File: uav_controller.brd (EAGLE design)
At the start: 100 x 80 mm, 26 parts, among them IC1 PIC16F877SO, U1 L298, U2 L298, U3 LCD-16X28X2

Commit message: Renamed some components
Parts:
- removed R2, R3, R4, R5, R6, R7, R8: (no value), SparkFun-Resistors:AXIAL-0.3EZ
- OSC: value (none) -> 8Mhz
- renumbered R9 to BKLT, U1 to HBRIDGE-FRONT, U2 to HBRIDGE-REAR, Y1 to OSC
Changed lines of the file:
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@@
 <element name="PWRIN" library="SparkFun-Passives" package="1X02" value="" x="67.31" y="67.31" rot="R270"/>
 <element name="R1" library="SparkFun-Resistors" package="AXIAL-0.3EZ" value="" x="33.02" y="49.53" rot="R90"/>
-<element name="R2" library="SparkFun-Resistors" package="AXIAL-0.3EZ" value="" x="-27.94" y="57.15"/>
-<element name="R3" library="SparkFun-Resistors" package="AXIAL-0.3EZ" value="" x="-38.1" y="57.15"/>
-<element name="R4" library="SparkFun-Resistors" package="AXIAL-0.3EZ" value="" x="-48.26" y="57.15"/>
-<element name="R5" library="SparkFun-Resistors" package="AXIAL-0.3EZ" value="" x="-17.78" y="60.96"/>
-<element name="R6" library="SparkFun-Resistors" package="AXIAL-0.3EZ" value="" x="-27.94" y="60.96"/>
-<element name="R7" library="SparkFun-Resistors" package="AXIAL-0.3EZ" value="" x="-38.1" y="60.96"/>
-<element name="R8" library="SparkFun-Resistors" package="AXIAL-0.3EZ" value="" x="-48.26" y="60.96"/>
-<element name="U1" library="SparkFun-PowerIC" package="MULTIWATT15" value="L298" x="58.42" y="30.48" rot="R270"/>
-<element name="U2" library="SparkFun-PowerIC" package="MULTIWATT15" value="L298" x="50.8" y="52.07" rot="R270"/>
+<element name="HBRIDGE-FRONT" library="SparkFun-PowerIC" package="MULTIWATT15" value="L298" x="58.42" y="30.48" rot="R270"/>
+<element name="HBRIDGE-REAR" library="SparkFun-PowerIC" package="MULTIWATT15" value="L298" x="50.8" y="52.07" rot="R270"/>
 <element name="U3" library="SparkFun-Displays" package="LCD-8X2" value="LCD-16X28X2" x="34.29" y="21.59" rot="MR180"/>
 <element name="7803?" library="SparkFun-PowerIC" package="TO-220-ALT" value="" x="48.26" y="68.58" rot="R270"/>
 <element name="7805" library="SparkFun-PowerIC" package="TO-220-ALT" value="" x="35.56" y="68.58" rot="R90"/>
-<element name="R9" library="pot" package="PT-10" value="" x="62.23" y="10.16" rot="MR180"/>
+<element name="BKLT" library="pot" package="PT-10" value="" x="62.23" y="10.16" rot="MR180"/>
 <element name="L3G4200D" library="SparkFun-Connectors" package="1X09_LOCK" value="M09LOCK" x="7.62" y="19.05" rot="R90"/>
 <element name="RANGE_UP" library="SparkFun-Connectors" package="JST-3-PTH" value="" x="2.54" y="48.26" rot="R90"/>
@@
 <element name="RANGE_FORE" library="SparkFun-Connectors" package="JST-3-PTH" value="" x="2.54" y="57.15" rot="R90"/>
 <element name="JP5" library="SparkFun-Connectors" package="1X03" value="" x="26.67" y="60.96"/>
-<element name="Y1" library="SparkFun-FreqCtrl" package="RESONATOR-PTH" value="" x="17.78" y="21.59"/>
+<element name="OSC" library="SparkFun-FreqCtrl" package="RESONATOR-PTH" value="8Mhz" x="17.78" y="21.59"/>
 </elements>
 <signals>
@@
 <contactref element="IC1" pad="34"/>
 <contactref element="IC1" pad="13"/>
-<contactref element="U1" pad="8"/>
-<contactref element="U2" pad="8"/>
+<contactref element="HBRIDGE-FRONT" pad="8"/>
+<contactref element="HBRIDGE-REAR" pad="8"/>
 <wire x1="40.64" y1="29.21" x2="30.48" y2="29.21" width="0.4064" layer="1"/>
 <wire x1="30.48" y1="29.21" x2="29.21" y2="27.94" width="0.4064" layer="1"/>
@@
 <contactref element="U3" pad="1"/>
 <contactref element="U3" pad="15"/>
-<contactref element="R9" pad="A"/>
+<contactref element="BKLT" pad="A"/>
 <wire x1="44.45" y1="7.86" x2="48.5" y2="7.86" width="0.4064" layer="16"/>
 <wire x1="48.5" y1="7.86" x2="55.88" y2="15.24" width="0.4064" layer="16"/>
@@
 <wire x1="6.35" y1="38.1" x2="7.62" y2="36.83" width="0.4064" layer="16"/>
 <wire x1="7.62" y1="36.83" x2="7.747" y2="36.83" width="0.4064" layer="16"/>
-<contactref element="Y1" pad="2"/>
+<contactref element="OSC" pad="2"/>
 <wire x1="17.78" y1="21.59" x2="25.4" y2="13.97" width="0.4064" layer="1"/>
 <wire x1="25.4" y1="13.97" x2="25.4" y2="8.89" width="0.4064" layer="1"/>
@@
 <contactref element="IC1" pad="12"/>
 <contactref element="R1" pad="P$2"/>
-<contactref element="U1" pad="9"/>
-<contactref element="U2" pad="9"/>
+<contactref element="HBRIDGE-FRONT" pad="9"/>
+<contactref element="HBRIDGE-REAR" pad="9"/>
 <wire x1="43.18" y1="31.75" x2="52.07" y2="31.75" width="0.4064" layer="1"/>
 <wire x1="43.18" y1="31.75" x2="41.91" y2="30.48" width="0.4064" layer="1"/>
@@
 </signal>
 <signal name="VCC">
-<contactref element="U1" pad="4"/>
-<contactref element="U2" pad="4"/>
+<contactref element="HBRIDGE-FRONT" pad="4"/>
+<contactref element="HBRIDGE-REAR" pad="4"/>
 <contactref element="PWRIN" pad="2"/>
 <contactref element="7803?" pad="IN"/>
@@
 </signal>
 <signal name="N$2">
-<contactref element="U1" pad="14"/>
+<contactref element="HBRIDGE-FRONT" pad="14"/>
 <contactref element="JP2" pad="2"/>
 <wire x1="61.11" y1="22.92" x2="71.06" y2="22.92" width="0.4064" layer="16"/>
@@
 <signal name="N$3">
 <contactref element="JP2" pad="1"/>
-<contactref element="U1" pad="13"/>
+<contactref element="HBRIDGE-FRONT" pad="13"/>
 <wire x1="56.03" y1="24.19" x2="69.91" y2="24.19" width="0.4064" layer="16"/>
 <wire x1="69.91" y1="24.19" x2="71.12" y2="25.4" width="0.4064" layer="16"/>
 </signal>
 <signal name="N$4">
-<contactref element="U1" pad="3"/>
+<contactref element="HBRIDGE-FRONT" pad="3"/>
 <contactref element="JP1" pad="2"/>
 <wire x1="56.03" y1="36.89" x2="63.44" y2="36.89" width="0.4064" layer="16"/>
@@
 <signal name="N$5">
 <contactref element="JP1" pad="1"/>
-<contactref element="U1" pad="2"/>
+<contactref element="HBRIDGE-FRONT" pad="2"/>
 <wire x1="61.11" y1="38.16" x2="64.71" y2="38.16" width="0.4064" layer="16"/>
 <wire x1="64.71" y1="38.16" x2="71.12" y2="31.75" width="0.4064" layer="16"/>
 </signal>
 <signal name="N$6">
-<contactref element="U2" pad="2"/>
+<contactref element="HBRIDGE-REAR" pad="2"/>
 <contactref element="JP3" pad="1"/>
 <wire x1="53.49" y1="59.75" x2="67.25" y2="59.75" width="0.4064" layer="1"/>
@@
 <signal name="N$7">
 <contactref element="JP3" pad="2"/>
-<contactref element="U2" pad="3"/>
+<contactref element="HBRIDGE-REAR" pad="3"/>
 <wire x1="48.41" y1="58.48" x2="65.98" y2="58.48" width="0.4064" layer="1"/>
 <wire x1="65.98" y1="58.48" x2="67.31" y2="57.15" width="0.4064" layer="1"/>
 </signal>
 <signal name="N$8">
-<contactref element="U2" pad="13"/>
+<contactref element="HBRIDGE-REAR" pad="13"/>
 <contactref element="JP4" pad="1"/>
 <wire x1="48.41" y1="45.78" x2="59.75" y2="45.78" width="0.4064" layer="1"/>
@@
 <signal name="N$9">
 <contactref element="JP4" pad="2"/>
-<contactref element="U2" pad="14"/>
+<contactref element="HBRIDGE-REAR" pad="14"/>
 <wire x1="53.49" y1="44.51" x2="61.02" y2="44.51" width="0.4064" layer="1"/>
 <wire x1="61.02" y1="44.51" x2="67.31" y2="50.8" width="0.4064" layer="1"/>
@@
 <signal name="FWD1">
 <contactref element="IC1" pad="36"/>
-<contactref element="U1" pad="5"/>
+<contactref element="HBRIDGE-FRONT" pad="5"/>
 <wire x1="40.64" y1="31.75" x2="41.91" y2="33.02" width="0.4064" layer="16"/>
 <wire x1="41.91" y1="33.02" x2="54.7" y2="33.02" width="0.4064" layer="16"/>
@@
 <signal name="FWD2">
 <contactref element="IC1" pad="37"/>
-<contactref element="U1" pad="7"/>
+<contactref element="HBRIDGE-FRONT" pad="7"/>
 <wire x1="43.18" y1="34.29" x2="53.55" y2="34.29" width="0.4064" layer="1"/>
 <wire x1="53.55" y1="34.29" x2="56.03" y2="31.81" width="0.4064" layer="1"/>
@@
 <signal name="FWD3">
 <contactref element="IC1" pad="38"/>
-<contactref element="U1" pad="10"/>
+<contactref element="HBRIDGE-FRONT" pad="10"/>
 <wire x1="61.11" y1="28" x2="59.63" y2="28" width="0.4064" layer="1"/>
 <wire x1="59.63" y1="28" x2="59.69" y2="29.21" width="0.4064" layer="1"/>
@@
 <signal name="FWD4">
 <contactref element="IC1" pad="39"/>
-<contactref element="U1" pad="12"/>
+<contactref element="HBRIDGE-FRONT" pad="12"/>
 <wire x1="61.11" y1="25.46" x2="58.36" y2="25.46" width="0.4064" layer="1"/>
 <wire x1="58.36" y1="25.46" x2="58.42" y2="27.94" width="0.4064" layer="1"/>
@@
 <signal name="RWD1">
 <contactref element="IC1" pad="41"/>
-<contactref element="U2" pad="5"/>
+<contactref element="HBRIDGE-REAR" pad="5"/>
 <wire x1="40.64" y1="36.83" x2="39.37" y2="35.56" width="0.4064" layer="16"/>
 <wire x1="39.37" y1="35.56" x2="34.29" y2="35.56" width="0.4064" layer="16"/>
@@
 <signal name="RWD2">
 <contactref element="IC1" pad="42"/>
-<contactref element="U2" pad="7"/>
+<contactref element="HBRIDGE-REAR" pad="7"/>
 <wire x1="38.1" y1="39.37" x2="38.1" y2="45.72" width="0.4064" layer="16"/>
 <wire x1="38.1" y1="45.72" x2="45.72" y2="53.34" width="0.4064" layer="16"/>
@@
 <signal name="RWD3">
 <contactref element="IC1" pad="43"/>
-<contactref element="U2" pad="10"/>
+<contactref element="HBRIDGE-REAR" pad="10"/>
 <wire x1="38.1" y1="36.83" x2="39.37" y2="38.1" width="0.4064" layer="16"/>
 <wire x1="39.37" y1="38.1" x2="39.37" y2="45.72" width="0.4064" layer="16"/>
@@
 <signal name="RWD4">
 <contactref element="IC1" pad="44"/>
-<contactref element="U2" pad="12"/>
+<contactref element="HBRIDGE-REAR" pad="12"/>
 <wire x1="35.56" y1="39.37" x2="35.56" y2="41.91" width="0.4064" layer="1"/>
 <wire x1="35.56" y1="41.91" x2="40.64" y2="46.99" width="0.4064" layer="1"/>
@@
 <contactref element="U3" pad="16"/>
 <contactref element="U3" pad="2"/>
-<contactref element="R9" pad="E"/>
+<contactref element="BKLT" pad="E"/>
 <wire x1="44.45" y1="5.32" x2="47.23" y2="5.32" width="0.4064" layer="16"/>
 <wire x1="47.23" y1="5.32" x2="54.61" y2="12.7" width="0.4064" layer="16"/>
@@
 <signal name="D_DIM">
 <contactref element="U3" pad="3"/>
-<contactref element="R9" pad="S"/>
+<contactref element="BKLT" pad="S"/>
 <wire x1="62.23" y1="5.08" x2="50.8" y2="5.08" width="0.4064" layer="16"/>
 <wire x1="50.8" y1="5.08" x2="49.53" y2="3.81" width="0.4064" layer="16"/>
@@
 </signal>
 <signal name="OSC2">
-<contactref element="Y1" pad="3"/>
+<contactref element="OSC" pad="3"/>
 <contactref element="IC1" pad="15"/>
 <wire x1="20.32" y1="21.59" x2="25.4" y2="26.67" width="0.4064" layer="16"/>
 </signal>
 <signal name="OSC1">
-<contactref element="Y1" pad="1"/>
+<contactref element="OSC" pad="1"/>
 <contactref element="IC1" pad="14"/>
 <wire x1="27.94" y1="29.21" x2="26.67" y2="27.94" width="0.4064" layer="16"/>

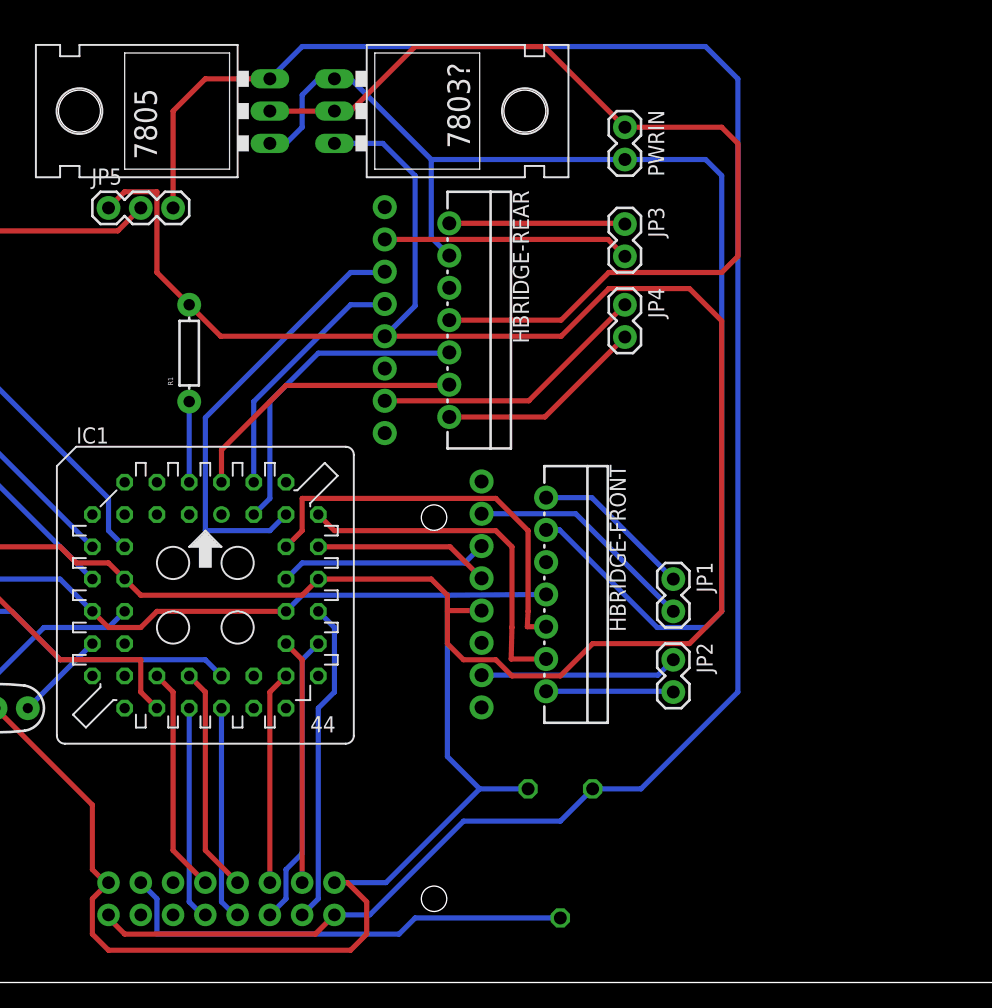
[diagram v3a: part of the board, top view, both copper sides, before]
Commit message: Adding board-interconnect https://www.sparkfun.com/products/10651 https://www.sparkfun.com/products/10647 https://www.sparkfun.com/products/10877
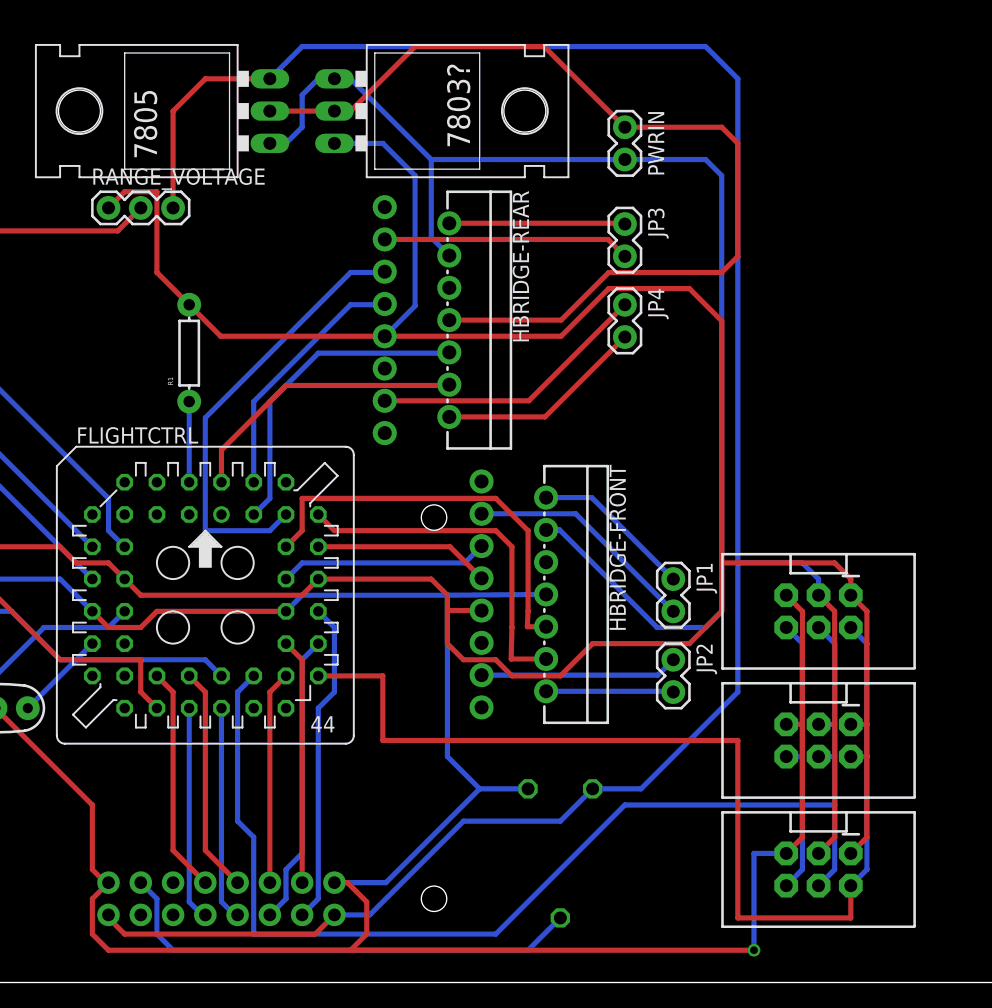
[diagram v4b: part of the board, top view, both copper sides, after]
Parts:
- added JP6, JP7: (no value), SparkFun-Connectors:2X3-SHROUDED
- added RANGE_VOLTAGE: (no value), SparkFun-Connectors:1X03
- JP5: device SparkFun-Connectors:1X03 -> SparkFun-Connectors:2X3-SHROUDED
- OSC: value 8Mhz -> 20Mhz
- moved JP5 69.8 mm to (82.5, 19.1), turned to 270 degrees
- renumbered IC1 to FLIGHTCTRL
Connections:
- removed net N$11: FLIGHTCTRL.27
- removed net N$12: FLIGHTCTRL.29
- new net N$15: JP5.6, JP6.6, JP7.6
- new net RX: FLIGHTCTRL.29, JP5.2, JP6.2, JP7.2
- new net TX: FLIGHTCTRL.27, JP5.4, JP6.4, JP7.4
- net 3.3V: now also JP6.1, JP7.1, RANGE_VOLTAGE.1
- net 5V: now also JP6.3, JP7.3, RANGE_VOLTAGE.3
- net GND: now also JP5.5, JP6.5, JP7.5
- net N$17: now also RANGE_VOLTAGE.2; no longer JP5.2
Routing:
- net TX: track 0.00 -> 93.9 mm
- net RX: track 0.00 -> 86.1 mm
- net GND: track 241.3 -> 305.9 mm, vias 0 -> 1
- net 3.3V: track 183.5 -> 218.1 mm
- net 5V: track 161.7 -> 192.5 mm
- net N$15: track 0.00 -> 22.6 mm
- net D_DIM: track 36.9 -> 37.9 mm
